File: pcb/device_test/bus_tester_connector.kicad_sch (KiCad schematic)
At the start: 5 parts, among them J301 Conn_01x05, J302 USB_A, J303 Conn_01x06

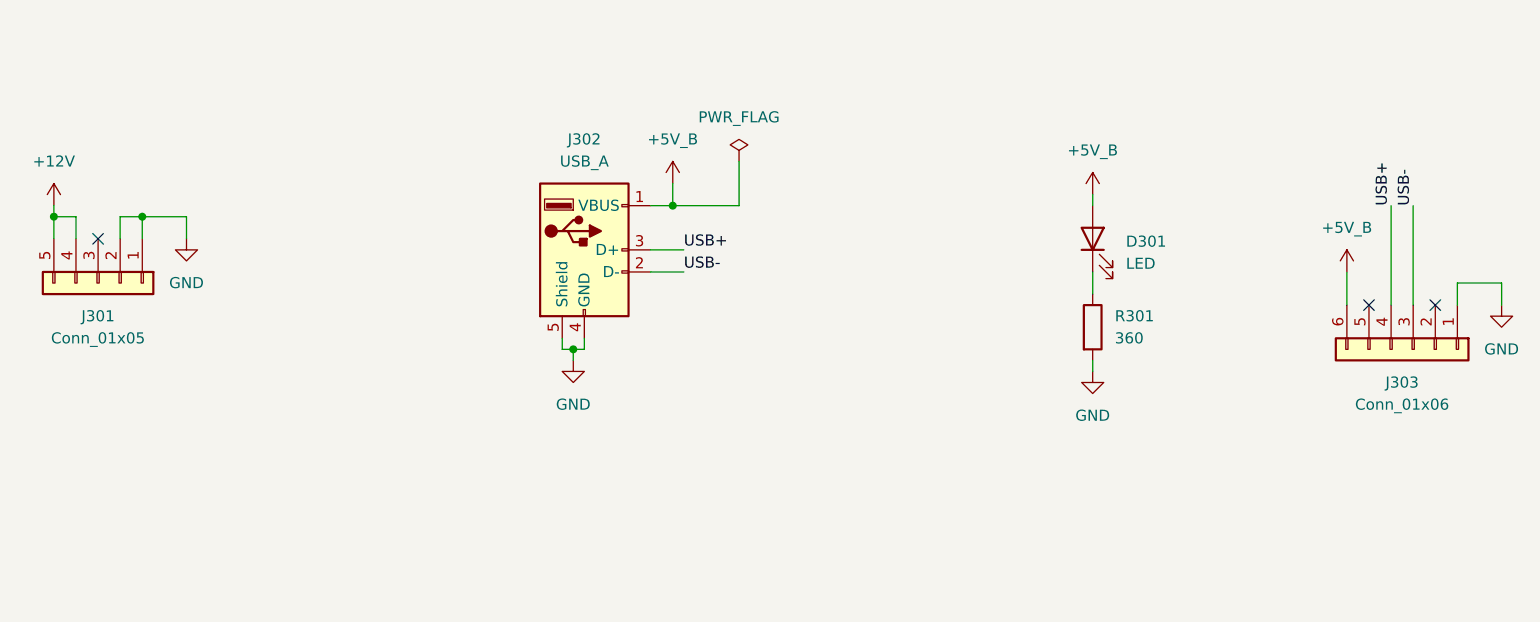
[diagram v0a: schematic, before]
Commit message: remove usb a, add usb c
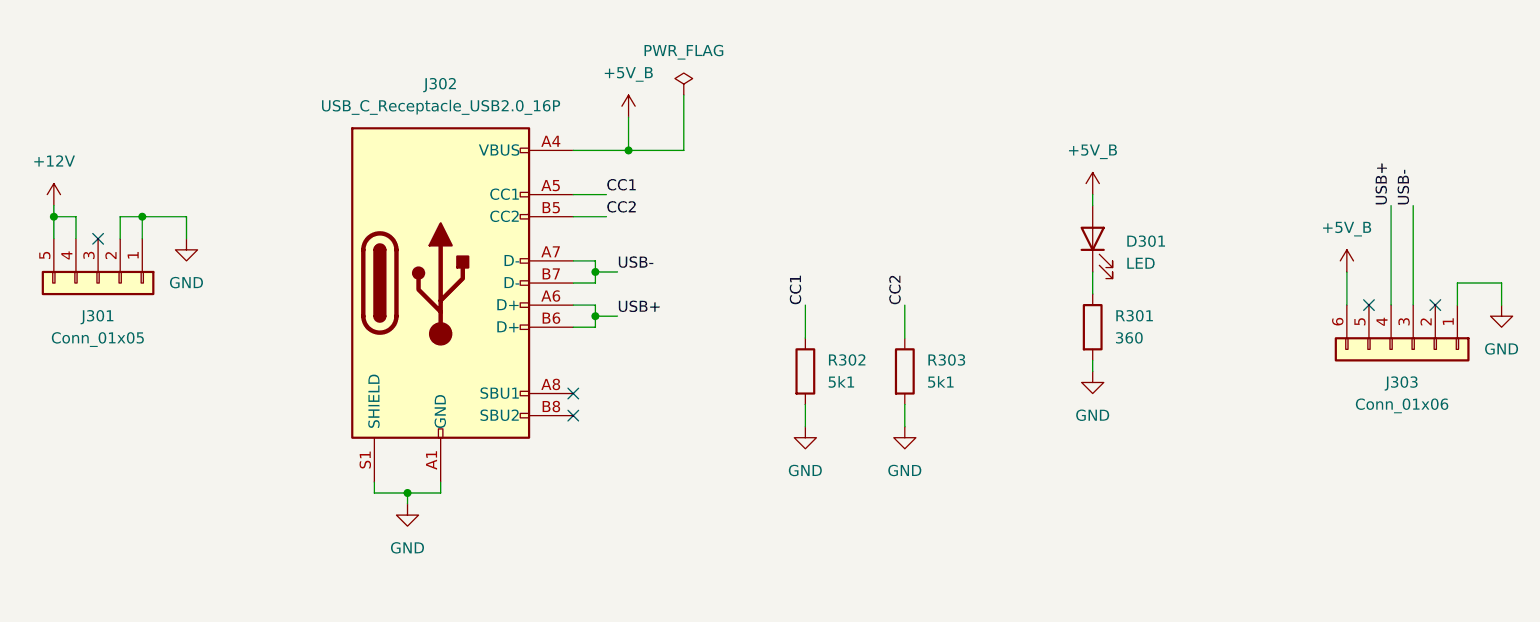
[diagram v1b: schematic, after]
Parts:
- removed J302: USB_A, Connector_USB:USB_A_Molex_67643_Horizontal, symbol Connector:USB_A
- added J302: USB_C_Receptacle_USB2.0_16P, Connector_USB:USB_C_Receptacle_G-Switch_GT-USB-7010ASV, symbol Connector:USB_C_Receptacle_USB2.0_16P
- added R302, R303: 5k1, Resistor_SMD:R_0805_2012Metric, symbol Device:R
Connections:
- net +5V_B: now also J302.A4 (VBUS), J302.A9 (VBUS), J302.B4 (VBUS), J302.B9 (VBUS)
- net GND: now also J302.A1 (GND), J302.A12 (GND), J302.B1 (GND), J302.B12 (GND), J302.S1 (SHIELD), R302.2, R303.2
- net USB+: now also J302.A6 (D+), J302.B6 (D+)
- net USB-: now also J302.A7 (D-), J302.B7 (D-)
- new net CC1: J302.A5 (CC1), R302.1
- new net CC2: J302.B5 (CC2), R303.1
- no-connect marks 3 -> 5

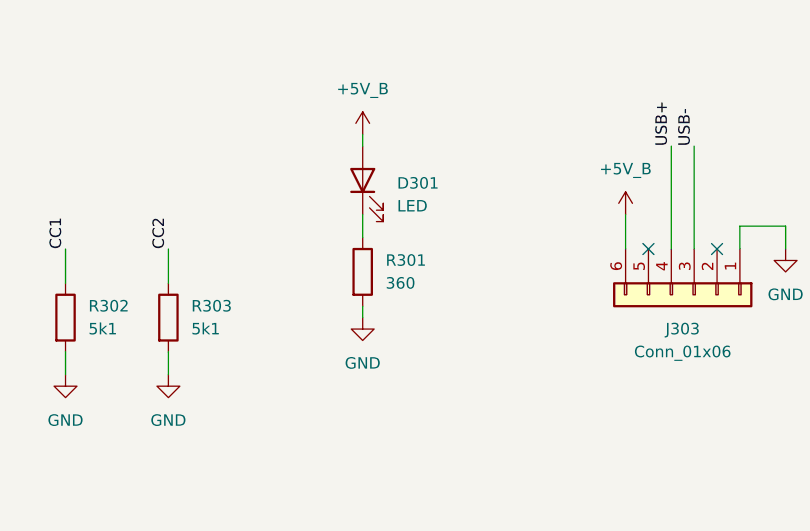
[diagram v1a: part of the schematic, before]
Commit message: update LCSC codes
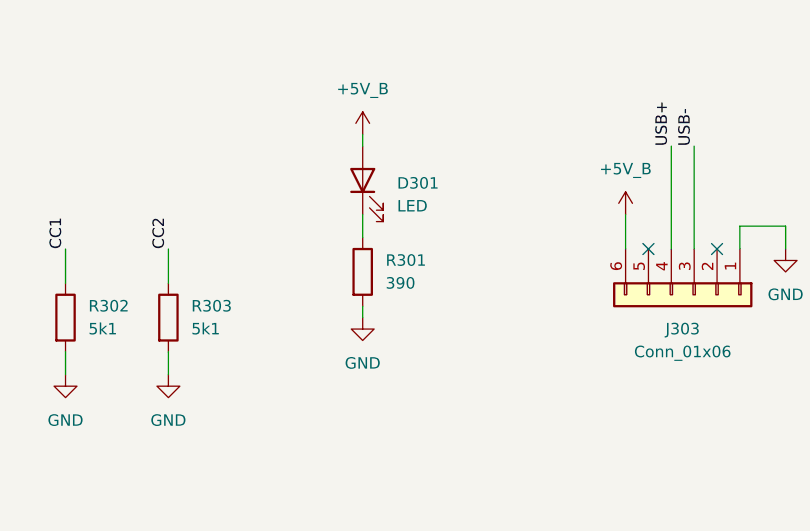
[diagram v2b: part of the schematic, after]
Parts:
- D301: LCSC (none) -> C84256
- J301: LCSC (none) -> C492413
- J303: LCSC (none) -> C492414
- R301: value 360 -> 390; LCSC (none) -> C17655
- R302, R303: LCSC (none) -> C27834
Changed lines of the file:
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@@
 			)
 		)
-		(property "LCSC" ""
+		(property "LCSC" "C492414"
 			(at 217.17 88.9 0)
 			(effects
@@
 			)
 		)
-		(property "Value" "360"
+		(property "Value" "390"
 			(at 182.88 87.6299 0)
 			(effects
@@
 			)
 		)
-		(property "LCSC" ""
+		(property "LCSC" "C17655"
 			(at 180.34 86.36 0)
 			(effects
@@
 			)
 		)
-		(property "LCSC" ""
+		(property "LCSC" "C492413"
 			(at 66.04 81.28 0)
 			(effects
@@
 			)
 		)
-		(property "LCSC" ""
+		(property "LCSC" "C27834"
 			(at 147.32 91.44 0)
 			(effects
@@
 			)
 		)
-		(property "LCSC" ""
+		(property "LCSC" "C84256"
 			(at 180.34 76.2 0)
 			(effects
@@
 			)
 		)
-		(property "LCSC" ""
+		(property "LCSC" "C27834"
 			(at 158.75 91.44 0)
 			(effects

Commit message: update device test pcb
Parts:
- removed J301: Conn_01x05, Connector_PinHeader_2.54mm:PinHeader_1x05_P2.54mm_Horizontal, symbol Connector_Generic:Conn_01x05
- removed J303: Conn_01x06, Connector_PinHeader_2.54mm:PinHeader_1x06_P2.54mm_Horizontal, symbol Connector_Generic:Conn_01x06
- added J302: Conn_02x10_Row_Letter_First, Connector_DIN:DIN41612_B3_2x10_Male_Horizontal_THT, symbol Connector_Generic:Conn_02x10_Row_Letter_First
- renumbered J302 to J301, R302 to R301, R303 to R302, R301 to R303
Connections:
- net +12V: now also J302.a1 (Pin_a1), J302.a2 (Pin_a2), J302.b1 (Pin_b1), J302.b2 (Pin_b2)
- net +5V_B: now also J302.a4 (Pin_a4), J302.a5 (Pin_a5), J302.b4 (Pin_b4), J302.b5 (Pin_b5)
- net GND: now also J302.a10 (Pin_a10), J302.a3 (Pin_a3), J302.b10 (Pin_b10), J302.b3 (Pin_b3)
- net USB+: now also J302.a6 (Pin_a6)
- net USB-: now also J302.b6 (Pin_b6)
- no-connect marks 5 -> 8
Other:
- moved on the sheet: D301, J301, R301, R302, R303

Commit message: update footprints and step's
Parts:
- J302: footprint Connector_DIN:DIN41612_B3_2x10_Male_Horizontal_THT -> USB:PCN10-20P-2.54DS
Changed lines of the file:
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@@
 	(label "USB-"
 		(at 201.93 90.17 0)
-		(fields_autoplaced yes)
 		(effects
 			(font
@@
 	(label "CC2"
 		(at 127 88.9 90)
-		(fields_autoplaced yes)
 		(effects
 			(font
@@
 	(label "USB-"
 		(at 93.98 85.09 0)
-		(fields_autoplaced yes)
 		(effects
 			(font
@@
 	(label "CC1"
 		(at 115.57 88.9 90)
-		(fields_autoplaced yes)
 		(effects
 			(font
@@
 	(label "CC1"
 		(at 92.71 76.2 0)
-		(fields_autoplaced yes)
 		(effects
 			(font
@@
 	(label "USB+"
 		(at 176.53 90.17 180)
-		(fields_autoplaced yes)
 		(effects
 			(font
@@
 	(label "USB+"
 		(at 93.98 90.17 0)
-		(fields_autoplaced yes)
 		(effects
 			(font
@@
 	(label "CC2"
 		(at 92.71 78.74 0)
-		(fields_autoplaced yes)
 		(effects
 			(font
@@
 			)
 		)
-		(property "Footprint" "Connector_DIN:DIN41612_B3_2x10_Male_Horizontal_THT"
+		(property "Footprint" "USB:PCN10-20P-2.54DS"
 			(at 187.96 87.63 0)
 			(effects

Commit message: update footprint lib name & change connector footprint
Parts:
- J302: footprint USB:PCN10-20P-2.54DS -> PRJ:PCN10C-20S-2.54DS
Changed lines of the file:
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@@
 			)
 		)
-		(property "Footprint" "USB:PCN10-20P-2.54DS"
+		(property "Footprint" "PRJ:PCN10C-20S-2.54DS"
 			(at 187.96 87.63 0)
 			(effects

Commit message: update
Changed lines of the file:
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@@
 	(wire
 		(pts
-			(xy 195.58 90.17) (xy 201.93 90.17)
+			(xy 195.58 90.17) (xy 208.28 90.17)
 		)
 		(stroke
@@
 	(wire
 		(pts
-			(xy 91.44 90.17) (xy 93.98 90.17)
+			(xy 91.44 90.17) (xy 99.06 90.17)
 		)
 		(stroke
@@
 	(wire
 		(pts
-			(xy 127 88.9) (xy 127 92.71)
+			(xy 127 86.36) (xy 127 92.71)
 		)
 		(stroke
@@
 	(wire
 		(pts
-			(xy 176.53 90.17) (xy 182.88 90.17)
+			(xy 170.18 90.17) (xy 182.88 90.17)
 		)
 		(stroke
@@
 	(wire
 		(pts
-			(xy 91.44 85.09) (xy 93.98 85.09)
+			(xy 91.44 85.09) (xy 99.06 85.09)
 		)
 		(stroke
@@
 	(wire
 		(pts
-			(xy 88.9 78.74) (xy 92.71 78.74)
+			(xy 88.9 78.74) (xy 95.25 78.74)
 		)
 		(stroke
@@
 	(wire
 		(pts
-			(xy 88.9 76.2) (xy 92.71 76.2)
-		)
-		(stroke
-			(width 0)
-			(type default)
-		)
-	)
-	(wire
-		(pts
-			(xy 115.57 88.9) (xy 115.57 92.71)
+			(xy 88.9 76.2) (xy 95.25 76.2)
+		)
+		(stroke
+			(width 0)
+			(type default)
+		)
+	)
+	(wire
+		(pts
+			(xy 115.57 86.36) (xy 115.57 92.71)
 		)
 		(stroke
@@
 	)
 	(label "USB-"
-		(at 201.93 90.17 0)
+		(at 208.28 90.17 180)
+		(effects
+			(font
+				(size 1.27 1.27)
+			)
+			(justify right bottom)
+		)
+	)
+	(label "CC2"
+		(at 127 86.36 270)
+		(effects
+			(font
+				(size 1.27 1.27)
+			)
+			(justify right bottom)
+		)
+	)
+	(label "USB-"
+		(at 99.06 85.09 180)
+		(effects
+			(font
+				(size 1.27 1.27)
+			)
+			(justify right bottom)
+		)
+	)
+	(label "CC1"
+		(at 115.57 86.36 270)
+		(effects
+			(font
+				(size 1.27 1.27)
+			)
+			(justify right bottom)
+		)
+	)
+	(label "CC1"
+		(at 95.25 76.2 180)
+		(effects
+			(font
+				(size 1.27 1.27)
+			)
+			(justify right bottom)
+		)
+	)
+	(label "USB+"
+		(at 170.18 90.17 0)
 		(effects
 			(font
@@
 		)
 	)
+	(label "USB+"
+		(at 99.06 90.17 180)
+		(effects
+			(font
+				(size 1.27 1.27)
+			)
+			(justify right bottom)
+		)
+	)
 	(label "CC2"
-		(at 127 88.9 90)
-		(effects
-			(font
-				(size 1.27 1.27)
-			)
-			(justify left bottom)
-		)
-	)
-	(label "USB-"
-		(at 93.98 85.09 0)
-		(effects
-			(font
-				(size 1.27 1.27)
-			)
-			(justify left bottom)
-		)
-	)
-	(label "CC1"
-		(at 115.57 88.9 90)
-		(effects
-			(font
-				(size 1.27 1.27)
-			)
-			(justify left bottom)
-		)
-	)
-	(label "CC1"
-		(at 92.71 76.2 0)
-		(effects
-			(font
-				(size 1.27 1.27)
-			)
-			(justify left bottom)
-		)
-	)
-	(label "USB+"
-		(at 176.53 90.17 180)
-		(effects
-			(font
-				(size 1.27 1.27)
-			)
-			(justify right bottom)
-		)
-	)
-	(label "USB+"
-		(at 93.98 90.17 0)
-		(effects
-			(font
-				(size 1.27 1.27)
-			)
-			(justify left bottom)
-		)
-	)
-	(label "CC2"
-		(at 92.71 78.74 0)
-		(effects
-			(font
-				(size 1.27 1.27)
-			)
-			(justify left bottom)
-		)
-	)
+		(at 95.25 78.74 180)
+		(effects
+			(font
+				(size 1.27 1.27)
+			)
+			(justify right bottom)
+		)
+	)

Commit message: add caps
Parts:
- added C301: 100u / 25V, Capacitor_Tantalum_SMD:CP_EIA-7343-43_Kemet-X_Pad2.25x2.55mm_HandSolder, symbol Device:C_Polarized
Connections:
- net +5V_B: now also C301.1
- net GND: now also C301.2
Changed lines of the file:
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@@
+	(wire
+		(pts
+			(xy 121.92 67.31) (xy 121.92 69.85)
+		)
+		(stroke
+			(width 0)
+			(type default)
+		)
+	)
 	(wire
 		(pts
@@
 		(pts
 			(xy 201.93 77.47) (xy 201.93 69.85)
+		)
+		(stroke
+			(width 0)
+			(type default)
+		)
+	)
+	(wire
+		(pts
+			(xy 121.92 57.15) (xy 121.92 59.69)
 		)
 		(stroke
@@
 	)
 	(symbol
+		(lib_id "power:+5V")
+		(at 121.92 57.15 0)
+		(unit 1)
+		(exclude_from_sim no)
+		(in_bom yes)
+		(on_board yes)
+		(dnp no)
+		(fields_autoplaced yes)
+		(property "Reference" "#PWR0313"
+			(at 121.92 60.96 0)
+			(effects
+				(font
+					(size 1.27 1.27)
+				)
+				(hide yes)
+			)
+		)
+		(property "Value" "+5V_B"
+			(at 121.92 52.07 0)
+			(effects
+				(font
+					(size 1.27 1.27)
+				)
+			)
+		)
+		(property "Footprint" ""
+			(at 121.92 57.15 0)
+			(effects
+				(font
+					(size 1.27 1.27)
+				)
+				(hide yes)
+			)
+		)
+		(property "Datasheet" ""
+			(at 121.92 57.15 0)
+			(effects
+				(font
+					(size 1.27 1.27)
+				)
+				(hide yes)
+			)
+		)
+		(property "Description" "Power symbol creates a global label with name \"+5V\""
+			(at 121.92 57.15 0)
+			(effects
+				(font
+					(size 1.27 1.27)
+				)
+				(hide yes)
+			)
+		)
+		(property "LCSC" ""
+			(at 121.92 57.15 0)
+			(effects
+				(font
+					(size 1.27 1.27)
+				)
+				(hide yes)
+			)
+		)
+		(pin "1"
+		)
+		(instances
+			(project "device_test"
+				(path "/5d20b266-567e-45c6-9e3e-145c2aea1daa/863e4a9e-7535-46fc-ad01-9a2c57fe0c12"
+					(reference "#PWR0313")
+					(unit 1)
+				)
+			)
+		)
+	)
+	(symbol
+		(lib_id "Device:C_Polarized")
+		(at 121.92 63.5 0)
+		(unit 1)
+		(exclude_from_sim no)
+		(in_bom yes)
+		(on_board yes)
+		(dnp no)
+		(fields_autoplaced yes)
+		(property "Reference" "C301"
+			(at 125.73 61.3409 0)
+			(effects
+				(font
+					(size 1.27 1.27)
+				)
+				(justify left)
+			)
+		)
+		(property "Value" "100u / 25V"
+			(at 125.73 63.8809 0)
+			(effects
+				(font
+					(size 1.27 1.27)
+				)
+				(justify left)
+			)
+		)
+		(property "Footprint" "Capacitor_Tantalum_SMD:CP_EIA-7343-43_Kemet-X_Pad2.25x2.55mm_HandSolder"
+			(at 122.8852 67.31 0)
+			(effects
+				(font
+					(size 1.27 1.27)
+				)
+				(hide yes)
+			)
+		)
+		(property "Datasheet" "~"
+			(at 121.92 63.5 0)
+			(effects
+				(font
+					(size 1.27 1.27)
+				)
+				(hide yes)
+			)
+		)
+		(property "Description" "Polarized capacitor"
+			(at 121.92 63.5 0)
+			(effects
+				(font
+					(size 1.27 1.27)
+				)
+				(hide yes)
+			)
+		)
+		(property "LCSC" "C7230"
+			(at 121.92 63.5 0)
+			(effects
+				(font
+					(size 1.27 1.27)
+				)
+				(hide yes)
+			)
+		)
+		(pin "2"
+		)
+		(pin "1"
+		)
+		(instances
+			(project "device_test"
+				(path "/5d20b266-567e-45c6-9e3e-145c2aea1daa/863e4a9e-7535-46fc-ad01-9a2c57fe0c12"
+					(reference "C301")
+					(unit 1)
+				)
+			)
+		)
+	)
+	(symbol
 		(lib_id "power:GND")
 		(at 198.12 102.87 0)
@@
 					(unit 1)
 				)
+			)
+		)
+	)
+	(symbol
+		(lib_id "power:GND")
+		(at 121.92 69.85 0)
+		(unit 1)
+		(exclude_from_sim no)
+		(in_bom yes)
+		(on_board yes)
+		(dnp no)
+		(fields_autoplaced yes)
+		(property "Reference" "#PWR0314"
+			(at 121.92 76.2 0)
+			(effects
+				(font
+					(size 1.27 1.27)
+				)
+				(hide yes)
+			)
+		)
+		(property "Value" "GND"
+			(at 121.92 74.93 0)
+			(effects
+				(font
+					(size 1.27 1.27)
+				)
+			)
+		)
+		(property "Footprint" ""
+			(at 121.92 69.85 0)
+			(effects
+				(font
+					(size 1.27 1.27)
+				)
+				(hide yes)
+			)
+		)
+		(property "Datasheet" ""
+			(at 121.92 69.85 0)
+			(effects
+				(font
+					(size 1.27 1.27)
+				)
+				(hide yes)
+			)
+		)
+		(property "Description" "Power symbol creates a global label with name \"GND\" , ground"
+			(at 121.92 69.85 0)
+			(effects
+				(font
+					(size 1.27 1.27)
+				)
+				(hide yes)
+			)
+		)
+		(pin "1"
+		)
+		(instances
+			(project "device_test"
+				(path "/5d20b266-567e-45c6-9e3e-145c2aea1daa/863e4a9e-7535-46fc-ad01-9a2c57fe0c12"
+					(reference "#PWR0314")
+					(unit 1)
+				)

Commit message: upgrade to kicad 9.0.0
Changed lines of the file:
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@@
 (kicad_sch
-	(version 20231120)
+	(version 20250114)
 	(generator "eeschema")
-	(generator_version "8.0")
+	(generator_version "9.0")
 	(paper "A4")
 	(title_block
@@
 			(at 143.51 87.63 0)
 			(effects
+				(font
+					(size 1.27 1.27)
+				)
+				(hide yes)
+			)
+		)
+		(property "Sim.Pins" "1=K 2=A"
+			(at 143.51 87.63 0)
+			(effects
